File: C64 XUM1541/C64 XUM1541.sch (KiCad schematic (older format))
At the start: 0 parts

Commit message: Basic module
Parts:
- added A1: Arduino_Pro_Micro, arduino_pro_micro:Arduino_Pro_Micro, symbol arduino_pro_micro:Arduino_Pro_Micro
- added D1: POWER, LEDs:LED_D5.0mm, symbol Device:LED
- added J1: C64_IEC, C64_IEC:C64_IEC, symbol C64_IEC:C64_IEC
- added R1: 330, Resistors_THT:R_Axial_DIN0207_L6.3mm_D2.5mm_P10.16mm_Horizontal, symbol Device:R
- added SW1: RESET, Buttons_Switches_THT:SW_Tactile_SPST_Angled_PTS645Vx39-2LFS, symbol Switch:SW_Push
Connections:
- new net: A1.22 (RST), SW1.1
- new net: D1.2 (A), R1.2
- new net ATN: A1.11 (D8), J1.3
- new net CLK: A1.15 (D14), J1.4
- new net DAT: A1.14 (D16), J1.5
- new net GND: A1.23 (GND), A1.3 (GND), A1.4 (GND), D1.1 (K), J1.2, J1.7, J1.8, SW1.2
- new net RST: A1.13 (D10), J1.6
- new net SRQ: A1.12 (D9), J1.1
- new net VCC: A1.21 (VCC), R1.1
- no-connect marks 0 -> 14
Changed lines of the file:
@@
 Comment4 ""
 $EndDescr
+$Comp
+L C64_IEC:C64_IEC J1
+U 1 1 5EDD9D01
+P 7200 3850
+F 0 "J1" H 7475 4175 50  0000 C CNN
+F 1 "C64_IEC" H 7475 4100 50  0000 C CNN
+F 2 "C64_IEC:C64_IEC" H 7200 3850 50  0001 C CNN
+F 3 "http://www.mouser.com/ds/2/18/40_c091_abd_e-75918.pdf" H 7200 3850 50  0001 C CNN
+	1    7200 3850
+	1    0    0    -1
+$EndComp
+$Comp
+L power:GND #PWR06
+U 1 1 5EDDCFBD
+P 6575 4025
+F 0 "#PWR06" H 6575 3775 50  0001 C CNN
+F 1 "GND" H 6580 3852 50  0000 C CNN
+F 2 "" H 6575 4025 50  0001 C CNN
+F 3 "" H 6575 4025 50  0001 C CNN
+	1    6575 4025
+	1    0    0    -1
+$EndComp
+Wire Wire Line
+	6575 4025 6575 3850
+Text GLabel 6825 3950 0    60   Input ~ 0
+CLK
+Wire Wire Line
+	6575 3850 6800 3850
+Wire Wire Line
+	6825 3950 6900 3950
+$Comp
+L power:GND #PWR07
+U 1 1 5EDE0044
+P 7825 4025
+F 0 "#PWR07" H 7825 3775 50  0001 C CNN
+F 1 "GND" H 7830 3852 50  0000 C CNN
+F 2 "" H 7825 4025 50  0001 C CNN
+F 3 "" H 7825 4025 50  0001 C CNN
+	1    7825 4025
+	-1   0    0    -1
+$EndComp
+Wire Wire Line
+	7825 4025 7825 3950
+Wire Wire Line
+	7825 3850 7600 3850
+Wire Wire Line
+	7500 3950 7825 3950
+Connection ~ 7825 3950
+Wire Wire Line
+	7825 3950 7825 3850
+Wire Wire Line
+	6825 3750 6900 3750
+Text GLabel 7200 4225 3    60   Input ~ 0
+ATN
+Wire Wire Line
+	7200 4225 7200 4150
+Text GLabel 7575 3750 2    60   Input ~ 0
+SRQ
+Wire Wire Line
+	7575 3750 7500 3750
+Text GLabel 7200 3475 1    60   Input ~ 0
+RST
+Wire Wire Line
+	7200 3475 7200 3550
+NoConn ~ 4300 3300
+NoConn ~ 4300 3400
+NoConn ~ 5250 3300
+Wire Wire Line
+	4775 4725 4775 4650
+$Comp
+L power:GND #PWR0101
+U 1 1 5EE04E5F
+P 4775 4800
+F 0 "#PWR0101" H 4775 4550 50  0001 C CNN
+F 1 "GND" H 4780 4627 50  0000 C CNN
+F 2 "" H 4775 4800 50  0001 C CNN
+F 3 "" H 4775 4800 50  0001 C CNN
+	1    4775 4800
+	1    0    0    -1
+$EndComp
+Wire Wire Line
+	4775 4725 4675 4725
+Wire Wire Line
+	4675 4725 4675 4650
+Wire Wire Line
+	4775 4725 4875 4725
+Wire Wire Line
+	4875 4725 4875 4650
+Connection ~ 4775 4725
+Wire Wire Line
+	4775 4725 4775 4800
+Wire Wire Line
+	4775 3050 4775 2975
+$Comp
+L arduino_pro_micro:Arduino_Pro_Micro A1
+U 1 1 5EDD95E8
+P 4775 3550
+F 0 "A1" H 5150 4050 50  0000 C CNN
+F 1 "Arduino_Pro_Micro" H 5150 3975 50  0000 C CNN
+F 2 "arduino_pro_micro:Arduino_Pro_Micro" H 4725 3550 50  0001 C CNN
+F 3 "~" H 4725 3550 50  0001 C CNN
+	1    4775 3550
+	1    0    0    -1
+$EndComp
+$Comp
+L power:VCC #PWR0102
+U 1 1 5EE06914
+P 4775 2975
+F 0 "#PWR0102" H 4775 2825 50  0001 C CNN
+F 1 "VCC" H 4792 3148 50  0000 C CNN
+F 2 "" H 4775 2975 50  0001 C CNN
+F 3 "" H 4775 2975 50  0001 C CNN
+	1    4775 2975
+	1    0    0    -1
+$EndComp
+Text GLabel 4225 4300 0    60   Input ~ 0
+ATN
+Wire Wire Line
+	4300 4300 4225 4300
+Text GLabel 4225 4400 0    60   Input ~ 0
+SRQ
+Wire Wire Line
+	4225 4400 4300 4400
+Text GLabel 5325 4400 2    60   Input ~ 0
+RST
+Wire Wire Line
+	5250 4400 5325 4400
+Text GLabel 5325 4300 2    60   Input ~ 0
+DAT
+Wire Wire Line
+	5250 4300 5325 4300
+Text GLabel 5325 4200 2    60   Input ~ 0
+CLK
+Wire Wire Line
+	5250 4200 5325 4200
+NoConn ~ 5250 3700
+NoConn ~ 5250 3800
+NoConn ~ 5250 3900
+NoConn ~ 5250 4000
+NoConn ~ 5250 4100
+NoConn ~ 4300 4200
+NoConn ~ 4300 4100
+NoConn ~ 4300 4000
+NoConn ~ 4300 3900
+NoConn ~ 4300 3800
+NoConn ~ 4300 3700
+Text GLabel 6825 3750 0    60   Input ~ 0
+DAT
+$Comp
+L Device:R R1
+U 1 1 5EE0FE5F
+P 6525 6975
+F 0 "R1" H 6595 7021 50  0000 L CNN
+F 1 "330" H 6595 6930 50  0000 L CNN
+F 2 "Resistors_THT:R_Axial_DIN0207_L6.3mm_D2.5mm_P10.16mm_Horizontal" V 6455 6975 50  0001 C CNN
+F 3 "~" H 6525 6975 50  0001 C CNN
+	1    6525 6975
+	1    0    0    -1
+$EndComp
+$Comp
+L Device:LED D1
+U 1 1 5EE10306
+P 6525 7275
+F 0 "D1" V 6564 7157 50  0000 R CNN
+F 1 "POWER" V 6473 7157 50  0000 R CNN
+F 2 "LEDs:LED_D5.0mm" H 6525 7275 50  0001 C CNN
+F 3 "~" H 6525 7275 50  0001 C CNN
+	1    6525 7275
+	0    -1   -1   0
+$EndComp
+$Comp
+L power:VCC #PWR0103
+U 1 1 5EE10D8F
+P 6525 6825
+F 0 "#PWR0103" H 6525 6675 50  0001 C CNN
+F 1 "VCC" H 6542 6998 50  0000 C CNN
+F 2 "" H 6525 6825 50  0001 C CNN
+F 3 "" H 6525 6825 50  0001 C CNN
+	1    6525 6825
+	1    0    0    -1
+$EndComp
+$Comp
+L power:GND #PWR0104
+U 1 1 5EE111F9
+P 6525 7500
+F 0 "#PWR0104" H 6525 7250 50  0001 C CNN
+F 1 "GND" H 6530 7327 50  0000 C CNN
+F 2 "" H 6525 7500 50  0001 C CNN
+F 3 "" H 6525 7500 50  0001 C CNN
+	1    6525 7500
+	1    0    0    -1
+$EndComp
+Wire Wire Line
+	6525 7500 6525 7425
+$Comp
+L Switch:SW_Push SW1
+U 1 1 5EE1232D
+P 5525 3500
+F 0 "SW1" H 5525 3750 50  0000 C CNN
+F 1 "RESET" H 5525 3675 50  0000 C CNN
+F 2 "Buttons_Switches_THT:SW_Tactile_SPST_Angled_PTS645Vx39-2LFS" H 5525 3700 50  0001 C CNN
+F 3 "~" H 5525 3700 50  0001 C CNN
+	1    5525 3500
+	1    0    0    -1
+$EndComp
+Wire Wire Line
+	5250 3500 5325 3500
+$Comp
+L power:GND #PWR0105
+U 1 1 5EE13E2C
+P 5800 3575
+F 0 "#PWR0105" H 5800 3325 50  0001 C CNN
+F 1 "GND" H 5805 3402 50  0000 C CNN
+F 2 "" H 5800 3575 50  0001 C CNN
+F 3 "" H 5800 3575 50  0001 C CNN
+	1    5800 3575
+	1    0    0    -1
+$EndComp
+Wire Wire Line
+	5800 3575 5800 3500
+Wire Wire Line
+	5725 3500 5800 3500
 $EndSCHEMATC

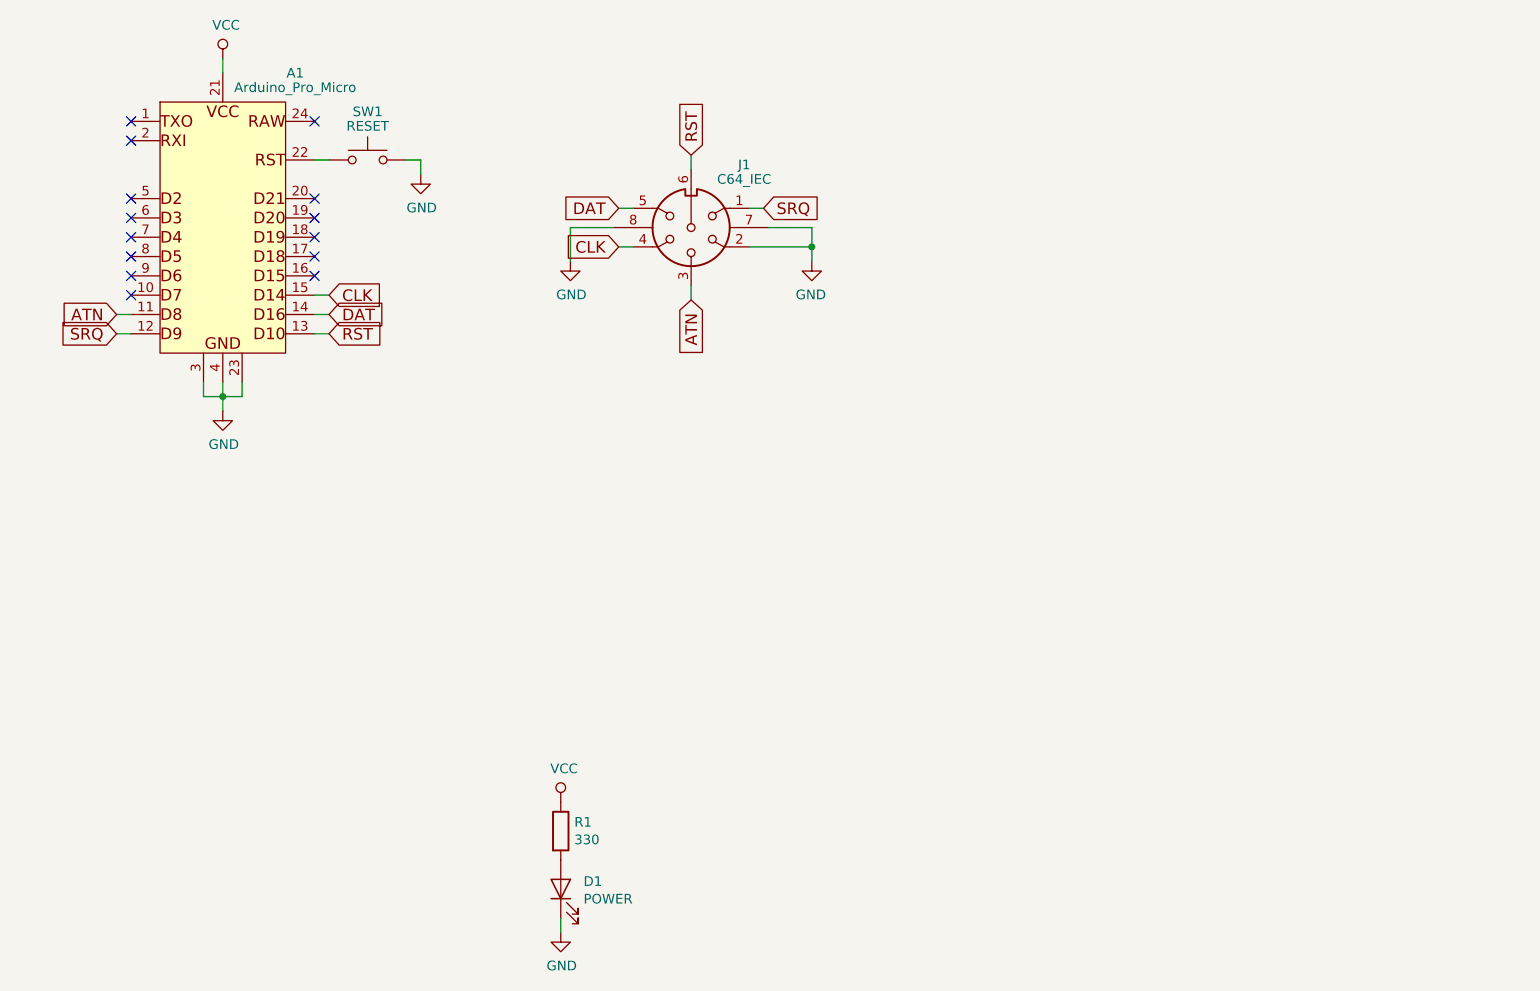
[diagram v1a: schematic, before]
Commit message: Added parallel header
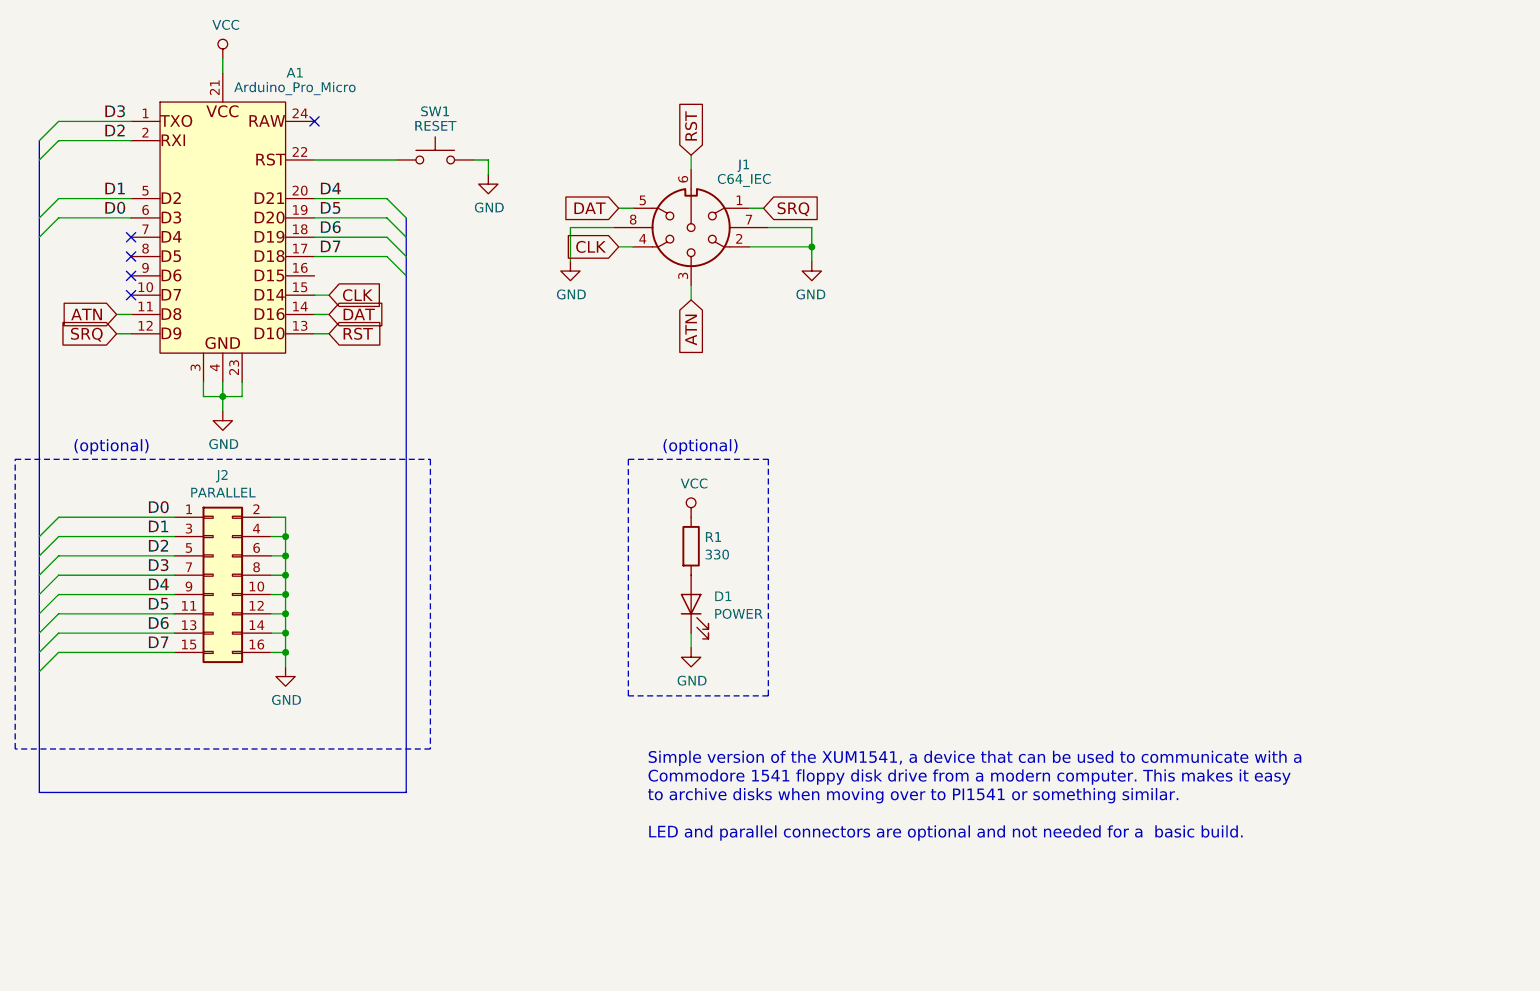
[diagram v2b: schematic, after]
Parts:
- added J2: PARALLEL, Pin_Headers:Pin_Header_Straight_2x08_Pitch2.54mm, symbol Connector_Generic:Conn_02x08_Odd_Even
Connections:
- net GND: now also J2.10 (Pin_10), J2.12 (Pin_12), J2.14 (Pin_14), J2.16 (Pin_16), J2.2 (Pin_2), J2.4 (Pin_4), J2.6 (Pin_6), J2.8 (Pin_8)
- net D3: now reaches A1.1 (TXO)
- net D3: now also J2.7 (Pin_7)
- net D7: now reaches A1.17 (D18)
- net D7: now also J2.15 (Pin_15)
- net D6: now reaches A1.18 (D19)
- net D6: now also J2.13 (Pin_13)
- net D5: now reaches A1.19 (D20)
- net D5: now also J2.11 (Pin_11)
- net D2: now reaches A1.2 (RXI)
- net D2: now also J2.5 (Pin_5)
- net D4: now reaches A1.20 (D21)
- net D4: now also J2.9 (Pin_9)
- net D1: now reaches A1.5 (D2)
- net D1: now also J2.3 (Pin_3)
- net D0: now reaches A1.6 (D3)
- net D0: now also J2.1 (Pin_1)
- no-connect marks 14 -> 5
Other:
- note added: "(optional)"
- note added: "Simple version of the XUM1541, a device that can be used to communicate with a\nCommodore 1541 floppy disk drive from a modern computer. This makes it easy\nto archive disks when moving over to PI1541 or something similar.\n\nLED and parallel connectors are optional and not needed for a basic build."
- moved on the sheet: D1, R1, SW1
